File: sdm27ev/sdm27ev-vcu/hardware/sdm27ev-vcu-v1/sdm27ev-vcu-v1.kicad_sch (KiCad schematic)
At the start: 3 parts, among them J1 6437288-1, J2 6437288-1, U1 ESP32-P4

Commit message: VCU sch updates
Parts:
- removed U1: ESP32-P4, SDM27 EV VCU:QFN-104_L10.0-W10.0-P0.35-TL-EP7.5, symbol EV VCU:ESP32-P4
- added C1, C2, C3, C5, C6: 100nF, Capacitor_SMD:C_0603_1608Metric, symbol Device:C_Small
- added C4: 10uF, Capacitor_SMD:C_0603_1608Metric, symbol Device:C_Small
- added R1, R2: 10k, Resistor_SMD:R_0603_1608Metric, symbol Device:R_Small
- added U1: ESP32-P4-Core, symbol SDM_EV:ESP32-P4-Core
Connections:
- new net: R2.1, U1.4 (EN_2V8)
- new net: R1.1, U1.6 (EN_1V8)
- new net 1.8V: C6.1, U1.7 (1V8OUT)
- new net 2.8V: C5.1, U1.5 (2V8OUT)
- new net 3.3V: C1.1, C2.1, C3.1, C4.1, R1.2, R2.2, U1.84 (RTC_VBAT), U1.85 (ESP_3V3), U1.86 (ESP_3V3)
- new net GND: C1.2, C2.2, C3.2, C4.2, C5.2, C6.2, U1.1 (GND), U1.15 (GND), U1.3 (GND), U1.33 (GND), U1.40 (GND), U1.47 (GND), U1.52 (GND), U1.83 (GND)
- no-connect marks 0 -> 1
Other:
- note added: "BULK"

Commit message: more VCU updates
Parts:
- added C7: 100nF, Capacitor_SMD:C_0603_1608Metric, symbol Device:C_Small
- added C8: 1uF, Capacitor_SMD:C_0603_1608Metric, symbol Device:C_Small
- added C9: 1uF 50V, Capacitor_SMD:C_0603_1608Metric, symbol Device:C_Small
- added IC1: TPD4E05U06QDQARQ1, DQA(R-PUSON-N10), symbol SDM_EV:TPD4E05U06QDQARQ1
- added J4: 2201778-1, 22017781, symbol SDM_EV:2201778-1
- added J5: USB4725-03-C-KIT, SDM_Misc:GCT_USB4730-GF-A_REVA, symbol SDM_MISC:USB4725-03-C-KIT
- added Q1: RRL035P03FRATR, RRL035P03FRATR, symbol SDM_EV:RRL035P03FRATR
- added R3: 10, Resistor_SMD:R_0603_1608Metric, symbol Device:R_Small
- added R4: 5.1k, Resistor_SMD:R_0603_1608Metric, symbol Device:R_Small
- added R5: 49.9k, Resistor_SMD:R_0603_1608Metric, symbol Device:R_Small
- added R50, R51: 27, Resistor_SMD:R_0402_1005Metric, symbol Device:R_Small
- added R6: 0, Resistor_SMD:R_0603_1608Metric, symbol Device:R_Small
- added R7, R8, R9: 10k, Resistor_SMD:R_0603_1608Metric, symbol Device:R_Small
- added U2: CH32V003JxMx, Package_SO:JEITA_SOIC-8_3.9x4.9mm_P1.27mm, symbol MCU_WCH_RiscV:CH32V003JxMx
- added U3: HUSB238, symbol SDM_EV:HUSB238
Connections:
- net 3.3V: now also C7.1, C8.1, J4.4 (VDD), R7.2, R8.2, R9.2
- net GND: now also C7.2, C8.2, C9.2, IC1.3 (GND_1), IC1.8 (GND_2), J4.11 (GND_1), J4.12 (GND_2), J4.13 (GND_3), J4.14 (GND_4), J4.15 (GND_5), J4.16 (GND_6), J4.6 (VSS), J5.A1 (GND), R6.2, U3.EP (GND)
- net at U1.48 (DM): now also R51.2
- net at U1.49 (DP): now also R50.1
- net P4_Boot: now reaches U1.62 (GPIO35)
- net P4_Boot: now also R8.1
- net at U1.63 (GPIO36): now also R7.1
- net SD1-DAT0: now reaches U1.67 (GPIO39)
- net SD1-DAT0: now also J4.7 (DAT0)
- net SD1-DAT1: now reaches U1.68 (GPIO40)
- net SD1-DAT1: now also J4.8 (DAT1)
- net SD1-DAT2: now reaches U1.69 (GPIO41)
- net SD1-DAT2: now also J4.1 (DAT2)
- net SD1-DAT3: now reaches U1.70 (GPIO42)
- net SD1-DAT3: now also J4.2 (CD/DAT3)
- net SD1-CLK: now reaches U1.71 (GPIO43)
- net SD1-CLK: now also J4.5 (CLK)
- net SD1-CMD: now reaches U1.72 (GPIO44)
- net SD1-CMD: now also J4.3 (CMD)
- net P4_Reset: now reaches U1.87 (CHIP_PU)
- net P4_Reset: now also R9.1
- new net: C9.1, R3.2, U3.1 (VIN)
- new net: R4.1, U3.10 (GATE)
- new net: IC1.4 (D2+), J5.A5 (CC1), U3.4 (CC1)
- new net: IC1.5 (D2-), J5.B5 (CC2), U3.5 (CC2)
- new net: R6.1, U3.9 (ISET)
- new net: Q1.3 (G), R4.2, R5.1
- new net: J5.A4 (VBUS), Q1.4 (S), R3.1, R5.2
- new net: IC1.10 (NC_3), IC1.6 (NC_4), IC1.7 (NC_1), IC1.9 (NC_2)
- new net SCL: U3.7 (SCL)
- new net SDA: U3.6 (SDA)
- new net USB_D+: IC1.1 (D1+), J5.A6 (D+), J5.B6 (D+), R50.2
- new net USB_D-: IC1.2 (D1-), J5.A7 (D-), J5.B7 (D-), R51.1
- new net VBUS: Q1.1 (D), Q1.2 (D_2), Q1.5 (D_3), Q1.6 (D_4)
- no-connect marks 1 -> 7
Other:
- moved on the sheet: C1, C2, C3, C4, C5, C6, J1, J2, R1, R2, U1

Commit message: Final VCU updates for the night
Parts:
- added C10: 1uF, Capacitor_SMD:C_0603_1608Metric, symbol Device:C_Small
- added C11, C13, C16: 100nF, Capacitor_SMD:C_0603_1608Metric, symbol Device:C_Small
- added C12: 10nF, Capacitor_SMD:C_0603_1608Metric, symbol Device:C_Small
- added C14, C15, C20: 10uF, Capacitor_SMD:C_0603_1608Metric, symbol Device:C_Small
- added C17: 100pF, Capacitor_SMD:C_0603_1608Metric, symbol Device:C_Small
- added C18, C19: 22uF, Capacitor_SMD:C_0603_1608Metric, symbol Device:C_Small
- added C21: 4.7uF, Capacitor_SMD:C_0603_1608Metric, symbol Device:C_Small
- added D1: VFHA1112H-3BZ2C-TR, LED_SMD:LED_0805_2012Metric, symbol Device:LED
- added IC2: TPS2121RUXR, SDM_Misc:TPS2121RUXR, symbol SDM_MISC:TPS2121RUXR
- added IC3: TPS56637RPAR, TPS56637RPAR, symbol SDM_EV:TPS56637RPAR
- added IC4: TPS61023DRLT, SOTFL50P160X60-6N, symbol SDM_EV:TPS61023DRLT
- added L1: 2.2uH, Inductor_SMD:L_7.3x7.3_H3.5, symbol Device:L_Small
- added L2: 1uH, Inductor_SMD:L_Changjiang_FTC404010S, symbol Device:L_Small
- added R10: 91, Resistor_SMD:R_0603_1608Metric, symbol Device:R_Small
- added R11: 10k, Resistor_SMD:R_0603_1608Metric, symbol Device:R_Small
- added R12: 750k, Resistor_SMD:R_0603_1608Metric, symbol Device:R_Small
- added R13: 100k, Resistor_SMD:R_0603_1608Metric, symbol Device:R_Small
- added R24: 10.2, Resistor_SMD:R_0402_1005Metric, symbol Device:R_Small
- added R25, R27, R28, R29, R31: 5k, Resistor_SMD:R_0402_1005Metric, symbol Device:R_Small
- added R26: 63.4k, Resistor_SMD:R_0402_1005Metric, symbol Device:R_Small
- added R30: 90.9k, Resistor_SMD:R_0402_1005Metric, symbol Device:R_Small
- added R32, R36: 20k, Resistor_SMD:R_0402_1005Metric, symbol Device:R_Small
- added R33: 10k, Resistor_SMD:R_0402_1005Metric, symbol Device:R_Small
- added R34: 45.3, Resistor_SMD:R_0402_1005Metric, symbol Device:R_Small
- added R35: 49.9, Resistor_SMD:R_0402_1005Metric, symbol Device:R_Small
- added SW1, SW2, SW3: SW_Push, Button_Switch_SMD:SW_SPST_CK_KXT3, symbol Switch:SW_Push
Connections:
- net 3.3V: now also U2.4 (VDD), C10.1, C11.1, C18.1, C19.1, C21.1, IC4.2 (EN), IC4.3 (VIN), L1.2, L2.1, R10.1, R11.1, R35.2
- net GND: now also U2.2 (VSS), C10.2, C11.2, C12.2, C20.2, C21.2, IC2.12 (GND), IC2.9 (ST), IC3.3 (AGND), IC4.4 (GND), R13.2, R25.1, R27.1, R29.1, R31.1, R32.1, R33.1, SW1.1, SW2.1, SW3.2
- net P4_Boot: now also U2.3 (PA2), SW2.2
- net P4_Reset: now also U2.7 (PC4), SW3.1
- net SCL: now also U2.6 (PC2)
- net SDA: now also U2.5 (PC1)
- net VBUS: now also IC2.2 (IN2), R28.2, R30.2
- net at U2.1 (PD6/PA1): now also D1.1 (K)
- net at U2.8 (PD1): now also R11.2, SW1.2
- new net: C13.2, IC3.6 (SW), R34.2, R35.1, R36.1
- new net: C17.1, R36.2
- new net: IC2.5 (OV1), R26.1, R27.2
- new net: IC2.6 (PR1), R24.1, R25.2
- new net: IC4.1 (FB), R12.2, R13.1
- new net: D1.2 (A), R10.2
- new net: C17.2, IC3.2 (FB), R33.2, R34.1
- new net: IC2.10 (ILIM), R32.2
- new net: C12.1, IC2.11 (SS)
- new net: IC2.3 (CP2), R28.1, R29.2
- new net: IC2.4 (OV2), R30.1, R31.2
- new net: C13.1, IC3.7 (BOOT), L1.1
- new net: IC4.5 (SW), L2.2
- new net 12V: IC2.7 (IN1), R24.2, R26.2
- new net 5V: C20.1, IC4.6 (VOUT), R12.1
- new net PGND: C14.2, C15.2, C16.2, C18.2, C19.2, IC3.9 (PGND)
- new net VCC: C14.1, C15.1, C16.1, IC2.1 (OUT_1), IC2.8 (OUT_2), IC3.1 (EN), IC3.11 (VIN_2), IC3.12 (VIN_3), IC3.13 (VIN_4), IC3.8 (VIN_1)
- no-connect marks 7 -> 9
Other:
- note added: "12V Priority"
- note added: "Analog 5V"
- note added: "Current limit 1.24A"
- note added: "IN1 overvoltage cutoff 15 V"
- note added: "IN2 overvoltage cutoff 21 V"
- note added: "PWR MUX"
- moved on the sheet: C1, C2, C3, C4, C5, C6, C7, C8, C9, IC1, J1, J2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

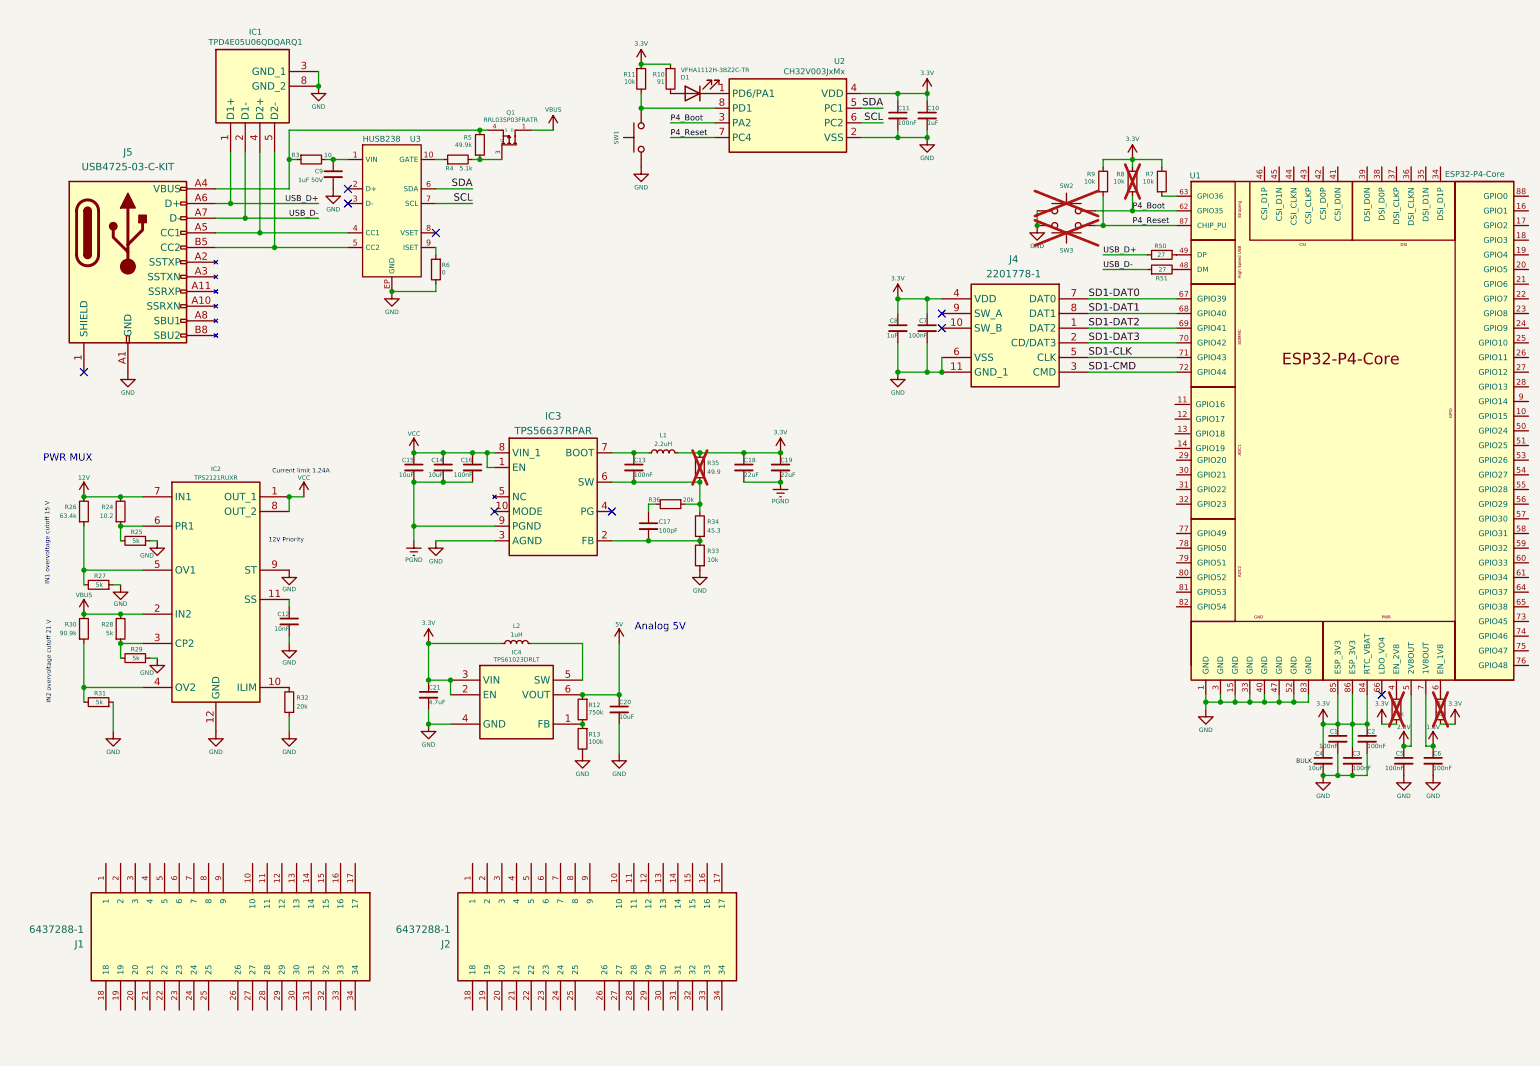
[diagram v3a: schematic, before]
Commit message: VCU edit, added hierarchical sheets and FD CAN circuitry
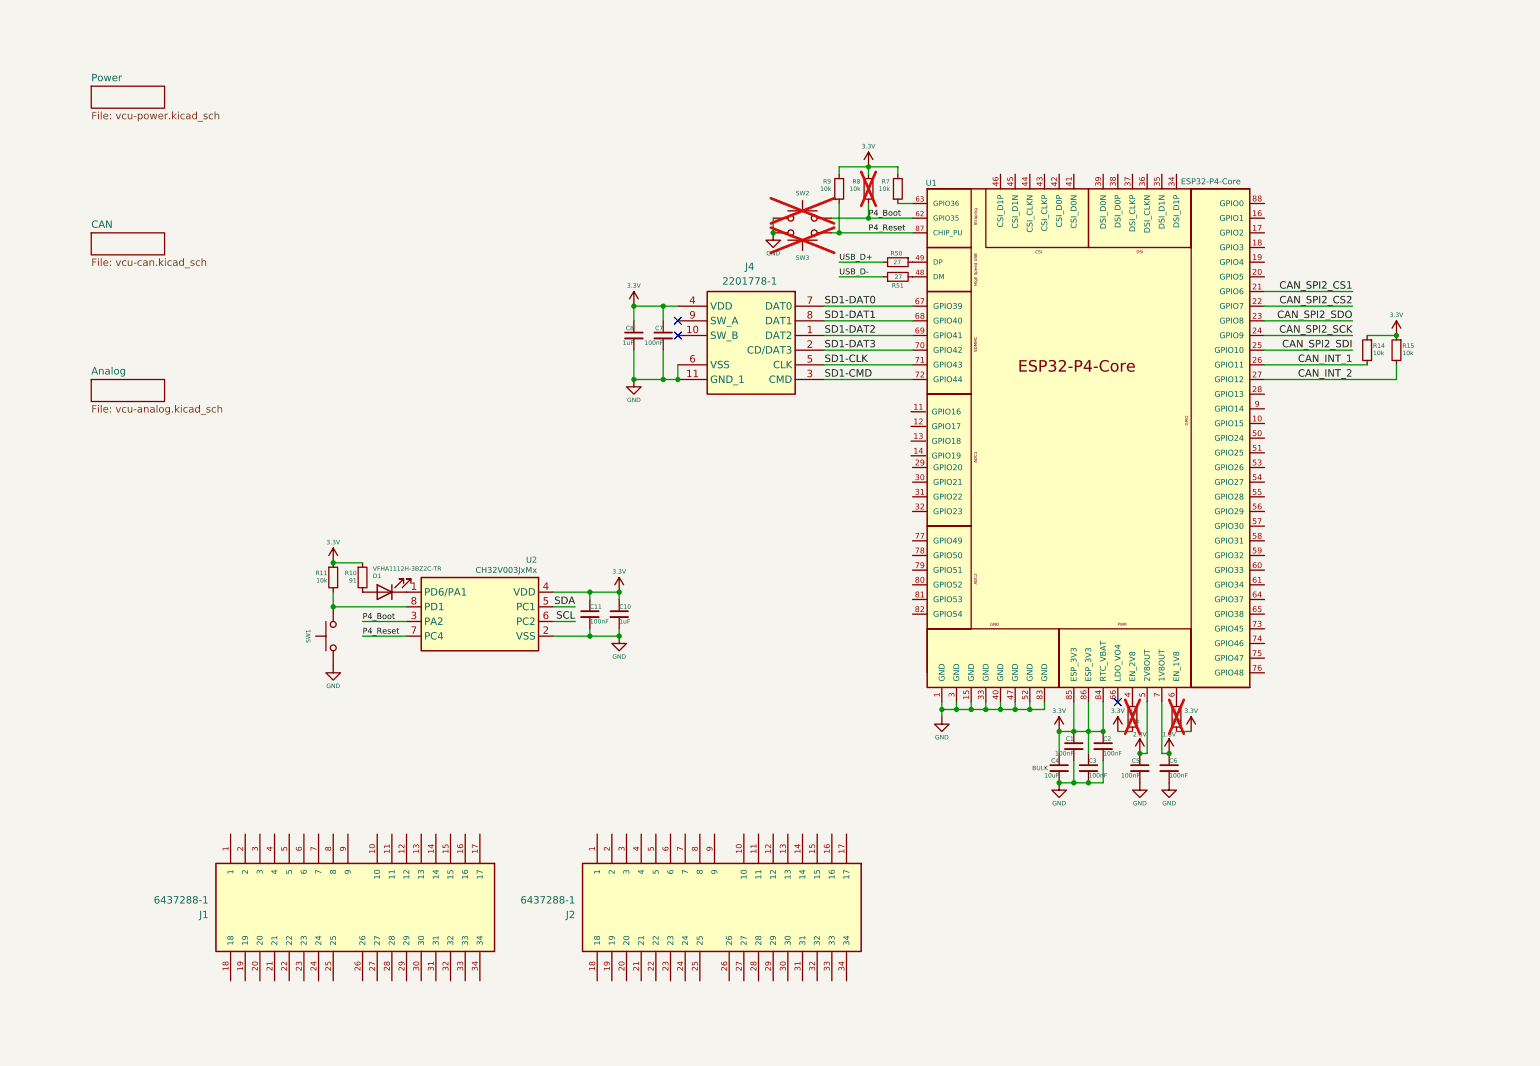
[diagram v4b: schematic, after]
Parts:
- removed C12: 10nF, Capacitor_SMD:C_0603_1608Metric, symbol Device:C_Small
- removed C13, C16: 100nF, Capacitor_SMD:C_0603_1608Metric, symbol Device:C_Small
- removed C14, C15, C20: 10uF, Capacitor_SMD:C_0603_1608Metric, symbol Device:C_Small
- removed C17: 100pF, Capacitor_SMD:C_0603_1608Metric, symbol Device:C_Small
- removed C18, C19: 22uF, Capacitor_SMD:C_0603_1608Metric, symbol Device:C_Small
- removed C21: 4.7uF, Capacitor_SMD:C_0603_1608Metric, symbol Device:C_Small
- removed C9: 1uF 50V, Capacitor_SMD:C_0603_1608Metric, symbol Device:C_Small
- removed IC1: TPD4E05U06QDQARQ1, DQA(R-PUSON-N10), symbol SDM_EV:TPD4E05U06QDQARQ1
- removed IC2: TPS2121RUXR, SDM_Misc:TPS2121RUXR, symbol SDM_MISC:TPS2121RUXR
- removed IC3: TPS56637RPAR, TPS56637RPAR, symbol SDM_EV:TPS56637RPAR
- removed IC4: TPS61023DRLT, SOTFL50P160X60-6N, symbol SDM_EV:TPS61023DRLT
- removed J5: USB4725-03-C-KIT, SDM_Misc:GCT_USB4730-GF-A_REVA, symbol SDM_MISC:USB4725-03-C-KIT
- removed L1: 2.2uH, Inductor_SMD:L_7.3x7.3_H3.5, symbol Device:L_Small
- removed L2: 1uH, Inductor_SMD:L_Changjiang_FTC404010S, symbol Device:L_Small
- removed Q1: RRL035P03FRATR, RRL035P03FRATR, symbol SDM_EV:RRL035P03FRATR
- removed R12: 750k, Resistor_SMD:R_0603_1608Metric, symbol Device:R_Small
- removed R13: 100k, Resistor_SMD:R_0603_1608Metric, symbol Device:R_Small
- removed R24: 10.2, Resistor_SMD:R_0402_1005Metric, symbol Device:R_Small
- removed R25, R27, R28, R29, R31: 5k, Resistor_SMD:R_0402_1005Metric, symbol Device:R_Small
- removed R26: 63.4k, Resistor_SMD:R_0402_1005Metric, symbol Device:R_Small
- removed R3: 10, Resistor_SMD:R_0603_1608Metric, symbol Device:R_Small
- removed R30: 90.9k, Resistor_SMD:R_0402_1005Metric, symbol Device:R_Small
- removed R32, R36: 20k, Resistor_SMD:R_0402_1005Metric, symbol Device:R_Small
- removed R33: 10k, Resistor_SMD:R_0402_1005Metric, symbol Device:R_Small
- removed R34: 45.3, Resistor_SMD:R_0402_1005Metric, symbol Device:R_Small
- removed R35: 49.9, Resistor_SMD:R_0402_1005Metric, symbol Device:R_Small
- removed R4: 5.1k, Resistor_SMD:R_0603_1608Metric, symbol Device:R_Small
- removed R5: 49.9k, Resistor_SMD:R_0603_1608Metric, symbol Device:R_Small
- removed R6: 0, Resistor_SMD:R_0603_1608Metric, symbol Device:R_Small
- removed U3: HUSB238, symbol SDM_EV:HUSB238
- added R14, R15: 10k, Resistor_SMD:R_0603_1608Metric, symbol Device:R_Small
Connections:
- net 3.3V: now also R14.1, R15.1
- net CAN_SPI2_CS1: now reaches U1.21 (GPIO6)
- net CAN_SPI2_CS2: now reaches U1.22 (GPIO7)
- net CAN_SPI2_SDO: now reaches U1.23 (GPIO8)
- net CAN_SPI2_SCK: now reaches U1.24 (GPIO9)
- net CAN_SPI2_SDI: now reaches U1.25 (GPIO10)
- net CAN_INT_1: now reaches U1.26 (GPIO11)
- net CAN_INT_1: now also R14.2
- net CAN_INT_2: now reaches U1.27 (GPIO12)
- net CAN_INT_2: now also R15.2
- no-connect marks 9 -> 3
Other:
- added sheet Analog (vcu-analog.kicad_sch)
- added sheet CAN (vcu-can.kicad_sch)
- added sheet Power (vcu-power.kicad_sch)
- note removed: "12V Priority"
- note removed: "Analog 5V"
- note removed: "Current limit 1.24A"
- note removed: "IN1 overvoltage cutoff 15 V"
- note removed: "IN2 overvoltage cutoff 21 V"
- note removed: "PWR MUX"
- moved on the sheet: C1, C10, C11, C2, C3, C4, C5, C6, C7, C8, D1, J1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

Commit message: added all hierarchical sheet pins, added can termination optocouplers
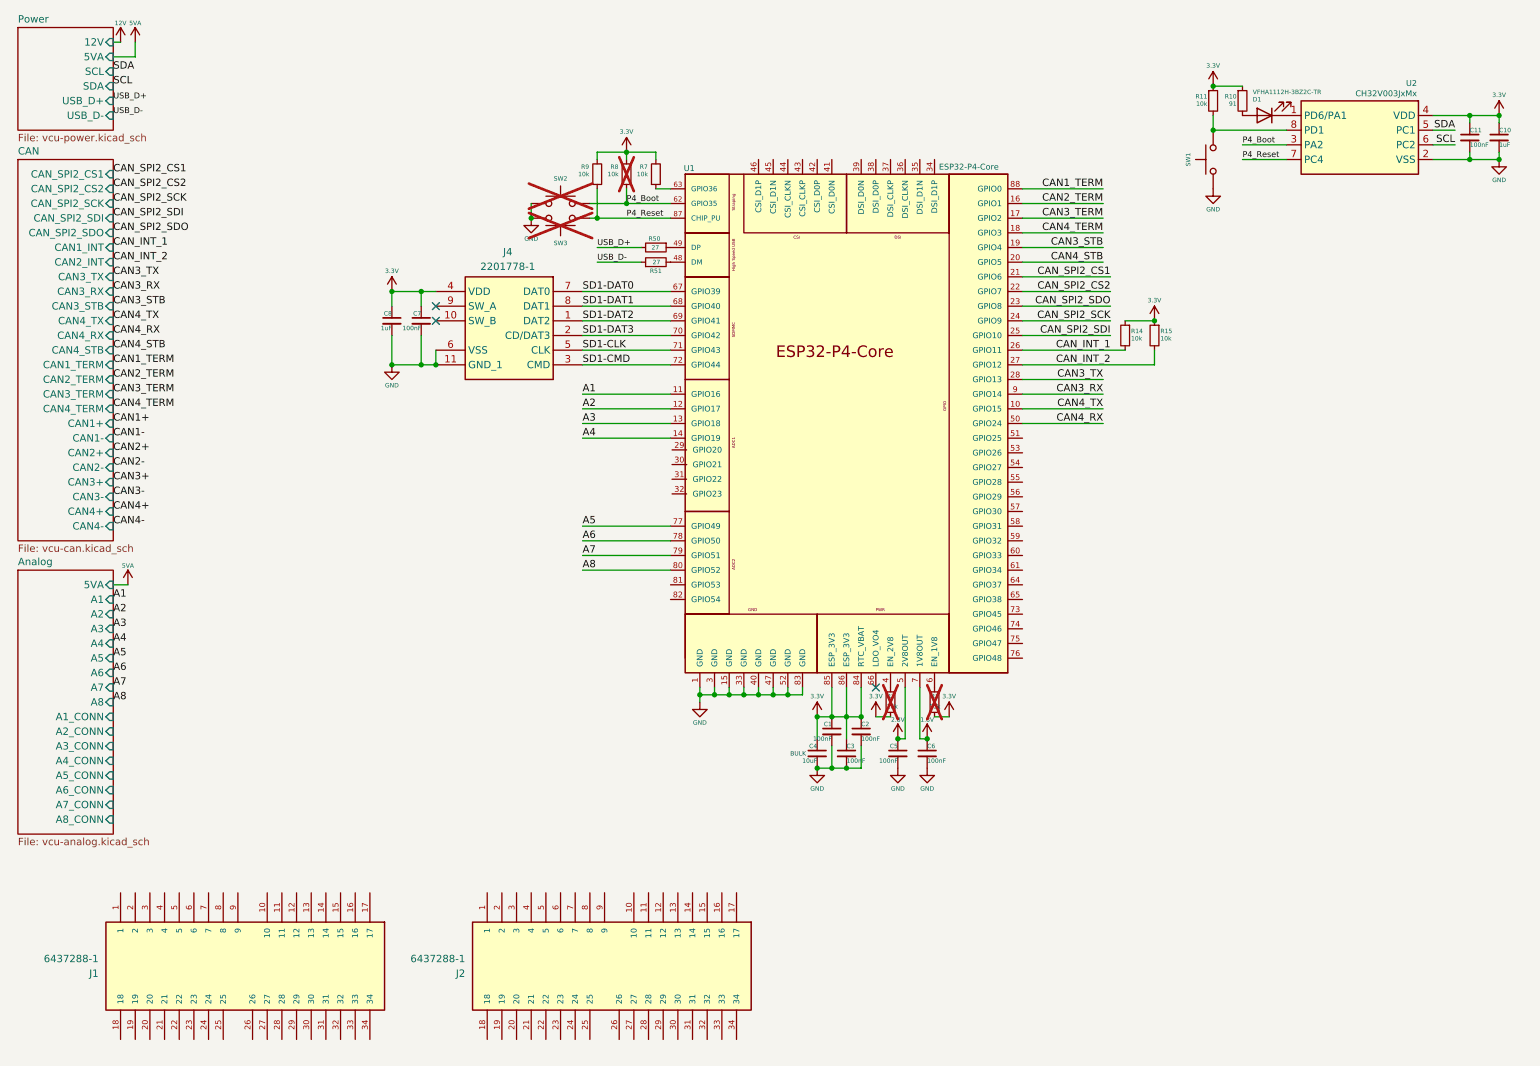
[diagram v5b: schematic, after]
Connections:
- net CAN4_TX: now reaches U1.10 (GPIO15)
- net A1: now reaches U1.11 (GPIO16)
- net A2: now reaches U1.12 (GPIO17)
- net A3: now reaches U1.13 (GPIO18)
- net A4: now reaches U1.14 (GPIO19)
- net CAN2_TERM: now reaches U1.16 (GPIO1)
- net CAN3_TERM: now reaches U1.17 (GPIO2)
- net CAN4_TERM: now reaches U1.18 (GPIO3)
- net CAN3_STB: now reaches U1.19 (GPIO4)
- net CAN4_STB: now reaches U1.20 (GPIO5)
- net CAN3_TX: now reaches U1.28 (GPIO13)
- net CAN4_RX: now reaches U1.50 (GPIO24)
- net A5: now reaches U1.77 (GPIO49)
- net A6: now reaches U1.78 (GPIO50)
- net A7: now reaches U1.79 (GPIO51)
- net A8: now reaches U1.80 (GPIO52)
- net CAN1_TERM: now reaches U1.88 (GPIO0)
- net CAN3_RX: now reaches U1.9 (GPIO14)
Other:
- sheet Analog ports: added 5VA, A1, A1_CONN, A2, A2_CONN, A3, A3_CONN, A4, A4_CONN, A5, A5_CONN, A6, A6_CONN, A7, A7_CONN, A8, A8_CONN; removed none
- sheet CAN ports: added CAN1+, CAN1-, CAN1_INT, CAN1_TERM, CAN2+, CAN2-, CAN2_INT, CAN2_TERM, CAN3+, CAN3-, CAN3_RX, CAN3_STB, CAN3_TERM, CAN3_TX, CAN4+, CAN4-, CAN4_RX, CAN4_STB, CAN4_TERM, CAN4_TX, CAN_SPI2_CS1, CAN_SPI2_CS2, CAN_SPI2_SCK, CAN_SPI2_SDI, CAN_SPI2_SDO; removed none
- sheet Power ports: added 12V, 5VA, SCL, SDA, USB_D+, USB_D-; removed none
- moved on the sheet: C1, C10, C11, C2, C3, C4, C5, C6, C7, C8, D1, J1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
